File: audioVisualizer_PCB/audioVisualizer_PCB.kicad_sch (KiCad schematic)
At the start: 26 parts, among them J1 Microphone_Module, J2 USB_B_Micro, J3 SPI_MATRIX, J4 JTAG, U1 STM32F103C8Tx, U2 HT7333, Y1 8Mhz

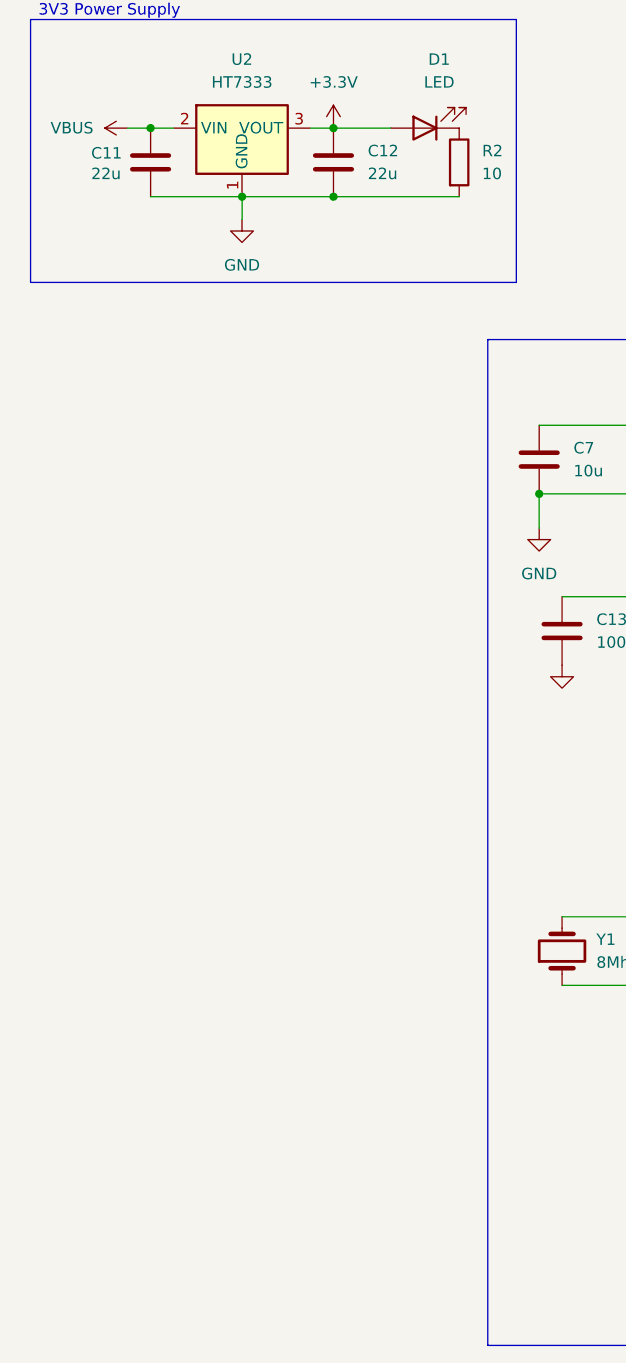
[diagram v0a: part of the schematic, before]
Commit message: Added additional omni-directional smd mic, not routed or programmed
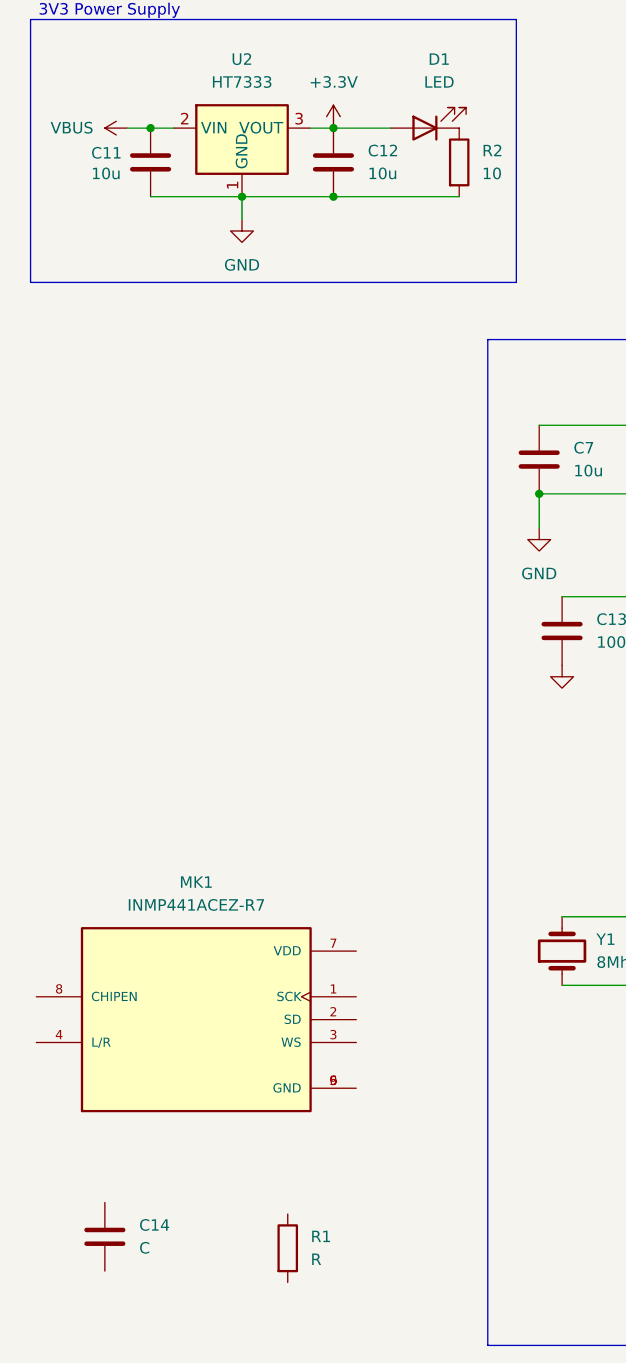
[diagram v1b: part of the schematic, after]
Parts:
- added C14: C, Capacitor_SMD:C_0805_2012Metric, symbol Device:C
- added MK1: INMP441ACEZ-R7, Microphone:MIC_INMP441ACEZ-R7, symbol Microphone:INMP441ACEZ-R7
- added R1: R, Resistor_SMD:R_0805_2012Metric, symbol Device:R
- C11, C12: value 22u -> 10u
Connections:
- new net: MK1.5 (GND), MK1.6 (GND), MK1.9 (GND)

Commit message: break em out
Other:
- added sheet MAX_Controller (MAX_Controller.kicad_sch)
- moved on the sheet: C14, MK1, R1
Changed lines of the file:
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@@
 	(symbol
 		(lib_id "Microphone:INMP441ACEZ-R7")
-		(at 36.83 128.27 0)
+		(at 41.91 93.98 0)
 		(unit 1)
 		(exclude_from_sim no)
@@
 		(fields_autoplaced yes)
 		(property "Reference" "MK1"
-			(at 36.83 113.03 0)
+			(at 41.91 78.74 0)
 			(effects
 				(font
@@
 		)
 		(property "Value" "INMP441ACEZ-R7"
-			(at 36.83 115.57 0)
+			(at 41.91 81.28 0)
 			(effects
 				(font
@@
 		)
 		(property "Footprint" "Microphone:MIC_INMP441ACEZ-R7"
-			(at 36.83 128.27 0)
+			(at 41.91 93.98 0)
 			(effects
 				(font
@@
 		)
 		(property "Datasheet" ""
-			(at 36.83 128.27 0)
+			(at 41.91 93.98 0)
 			(effects
 				(font
@@
 		)
 		(property "Description" ""
-			(at 36.83 128.27 0)
+			(at 41.91 93.98 0)
 			(effects
 				(font
@@
 		)
 		(property "MF" "TDK InvenSense"
-			(at 36.83 128.27 0)
+			(at 41.91 93.98 0)
 			(effects
 				(font
@@
 		)
 		(property "MAXIMUM_PACKAGE_HEIGHT" "1.05 mm"
-			(at 36.83 128.27 0)
+			(at 41.91 93.98 0)
 			(effects
 				(font
@@
 		)
 		(property "Package" "LGA-9 TDK InvenSense"
-			(at 36.83 128.27 0)
+			(at 41.91 93.98 0)
 			(effects
 				(font
@@
 		)
 		(property "Price" "None"
-			(at 36.83 128.27 0)
+			(at 41.91 93.98 0)
 			(effects
 				(font
@@
 		)
 		(property "Check_prices" "https://www.snapeda.com/parts/INMP441ACEZ-R7/TDK/view-part/?ref=eda"
-			(at 36.83 128.27 0)
+			(at 41.91 93.98 0)
 			(effects
 				(font
@@
 		)
 		(property "STANDARD" "Manufacturer Recommendations"
-			(at 36.83 128.27 0)
+			(at 41.91 93.98 0)
 			(effects
 				(font
@@
 		)
 		(property "PARTREV" "1.1"
-			(at 36.83 128.27 0)
+			(at 41.91 93.98 0)
 			(effects
 				(font
@@
 		)
 		(property "SnapEDA_Link" "https://www.snapeda.com/parts/INMP441ACEZ-R7/TDK/view-part/?ref=snap"
-			(at 36.83 128.27 0)
+			(at 41.91 93.98 0)
 			(effects
 				(font
@@
 		)
 		(property "MP" "INMP441ACEZ-R7"
-			(at 36.83 128.27 0)
+			(at 41.91 93.98 0)
 			(effects
 				(font
@@
 		)
 		(property "Description_1" "60 Hz ~ 15 kHz Digital, I2S Microphone MEMS (Silicon) 1.62 V ~ 3.63 V Omnidirectional (-26dB ±3dB @ 94dB SPL) Solder Pads"
-			(at 36.83 128.27 0)
+			(at 41.91 93.98 0)
 			(effects
 				(font
@@
 		)
 		(property "Availability" "In Stock"
-			(at 36.83 128.27 0)
+			(at 41.91 93.98 0)
 			(effects
 				(font
@@
 		)
 		(property "MANUFACTURER" "TDK InvenSense"
-			(at 36.83 128.27 0)
+			(at 41.91 93.98 0)
 			(effects
 				(font
@@
 	(symbol
 		(lib_id "Device:C")
-		(at 26.67 152.4 0)
+		(at 31.75 118.11 0)
 		(unit 1)
 		(exclude_from_sim no)
@@
 		(fields_autoplaced yes)
 		(property "Reference" "C14"
-			(at 30.48 151.1299 0)
+			(at 35.56 116.8399 0)
 			(effects
 				(font
@@
 		)
 		(property "Value" "C"
-			(at 30.48 153.6699 0)
+			(at 35.56 119.3799 0)
 			(effects
 				(font
@@
 		)
 		(property "Footprint" "Capacitor_SMD:C_0805_2012Metric"
-			(at 27.6352 156.21 0)
+			(at 32.7152 121.92 0)
 			(effects
 				(font
@@
 		)
 		(property "Datasheet" "~"
-			(at 26.67 152.4 0)
+			(at 31.75 118.11 0)
 			(effects
 				(font
@@
 		)
 		(property "Description" "Unpolarized capacitor"
-			(at 26.67 152.4 0)
+			(at 31.75 118.11 0)
 			(effects
 				(font
@@
 	(symbol
 		(lib_id "Device:R")
-		(at 46.99 153.67 0)
+		(at 52.07 119.38 0)
 		(unit 1)
 		(exclude_from_sim no)
@@
 		(fields_autoplaced yes)
 		(property "Reference" "R1"
-			(at 49.53 152.3999 0)
+			(at 54.61 118.1099 0)
 			(effects
 				(font
@@
 		)
 		(property "Value" "R"
-			(at 49.53 154.9399 0)
+			(at 54.61 120.6499 0)
 			(effects
 				(font
@@
 		)
 		(property "Footprint" "Resistor_SMD:R_0805_2012Metric"
-			(at 45.212 153.67 90)
+			(at 50.292 119.38 90)
 			(effects
 				(font
@@
 		)
 		(property "Datasheet" "~"
-			(at 46.99 153.67 0)
+			(at 52.07 119.38 0)
 			(effects
 				(font
@@
 		)
 		(property "Description" "Resistor"
-			(at 46.99 153.67 0)
+			(at 52.07 119.38 0)
 			(effects
 				(font
@@
 				)
 			)
+		)
+	)
+	(sheet
+		(at 29.21 132.08)
+		(size 26.67 22.86)
+		(exclude_from_sim no)
+		(in_bom yes)
+		(on_board yes)
+		(dnp no)
+		(fields_autoplaced yes)
+		(stroke
+			(width 0.1524)
+			(type solid)
+		)
+		(fill
+			(color 0 0 0 0.0000)
+		)
+		(property "Sheetname" "MAX_Controller"
+			(at 29.21 131.3684 0)
+			(effects
+				(font
+					(size 1.27 1.27)
+				)
+				(justify left bottom)
+			)
+		)
+		(property "Sheetfile" "MAX_Controller.kicad_sch"
+			(at 29.21 155.5246 0)
+			(effects
+				(font
+					(size 1.27 1.27)
+				)
+				(justify left top)
+			)
+		)
+		(instances
+			(project "audioVisualizer_PCB"
+				(path "/8779f4c0-fa76-4e9c-9285-12099bba0fb4"
+					(page "2")
+				)
+			)

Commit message: embeddeding the mcu is harder than I thought
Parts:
- removed C2: 20p, Capacitor_SMD:C_0805_2012Metric, symbol Device:C
- removed U1: STM32F103C8Tx, Package_QFP:LQFP-48_7x7mm_P0.5mm, symbol MCU_ST_STM32F1:STM32F103C8Tx
- removed Y1: 8Mhz, Crystal:Crystal_HC49-4H_Vertical, symbol Device:Crystal
- added U7: STM32F401CCUx, Package_DFN_QFN:QFN-48-1EP_7x7mm_P0.5mm_EP5.6x5.6mm, symbol MCU_ST_STM32F4:STM32F401CCUx
- added Y2: Crystal_GND23, Crystal:Crystal_SMD_3225-4Pin_3.2x2.5mm, symbol Device:Crystal_GND23
- C1: value 20p -> 15pF; footprint Capacitor_SMD:C_0805_2012Metric -> (none)
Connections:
- net +3.3V: now also U7.1 (VBAT), U7.24 (VDD), U7.36 (VDD), U7.48 (VDD), Y2.1, Y2.4
- net GND: now also C1.2, U7.23 (VSS), U7.35 (VSS), U7.47 (VSS), U7.49 (VSS), U7.8 (VSSA); no longer C1.1
- new net: C1.1, U7.5 (PH0), Y2.3 (G)

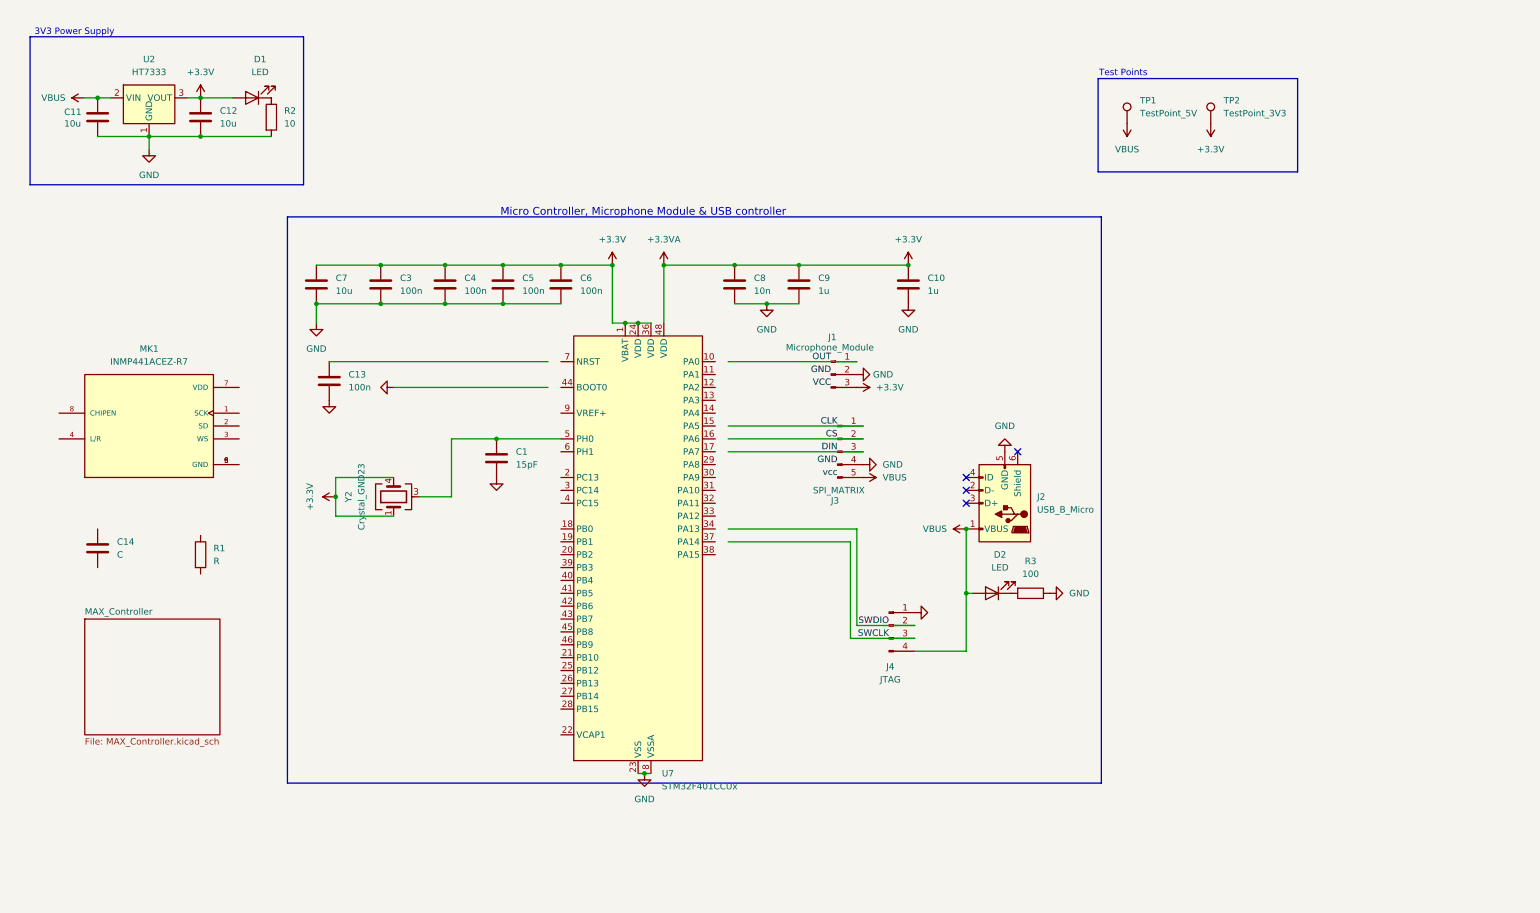
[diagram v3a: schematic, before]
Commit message: added stereo mics; setup usb-c;fixed timer issue for led matrix; using external clock
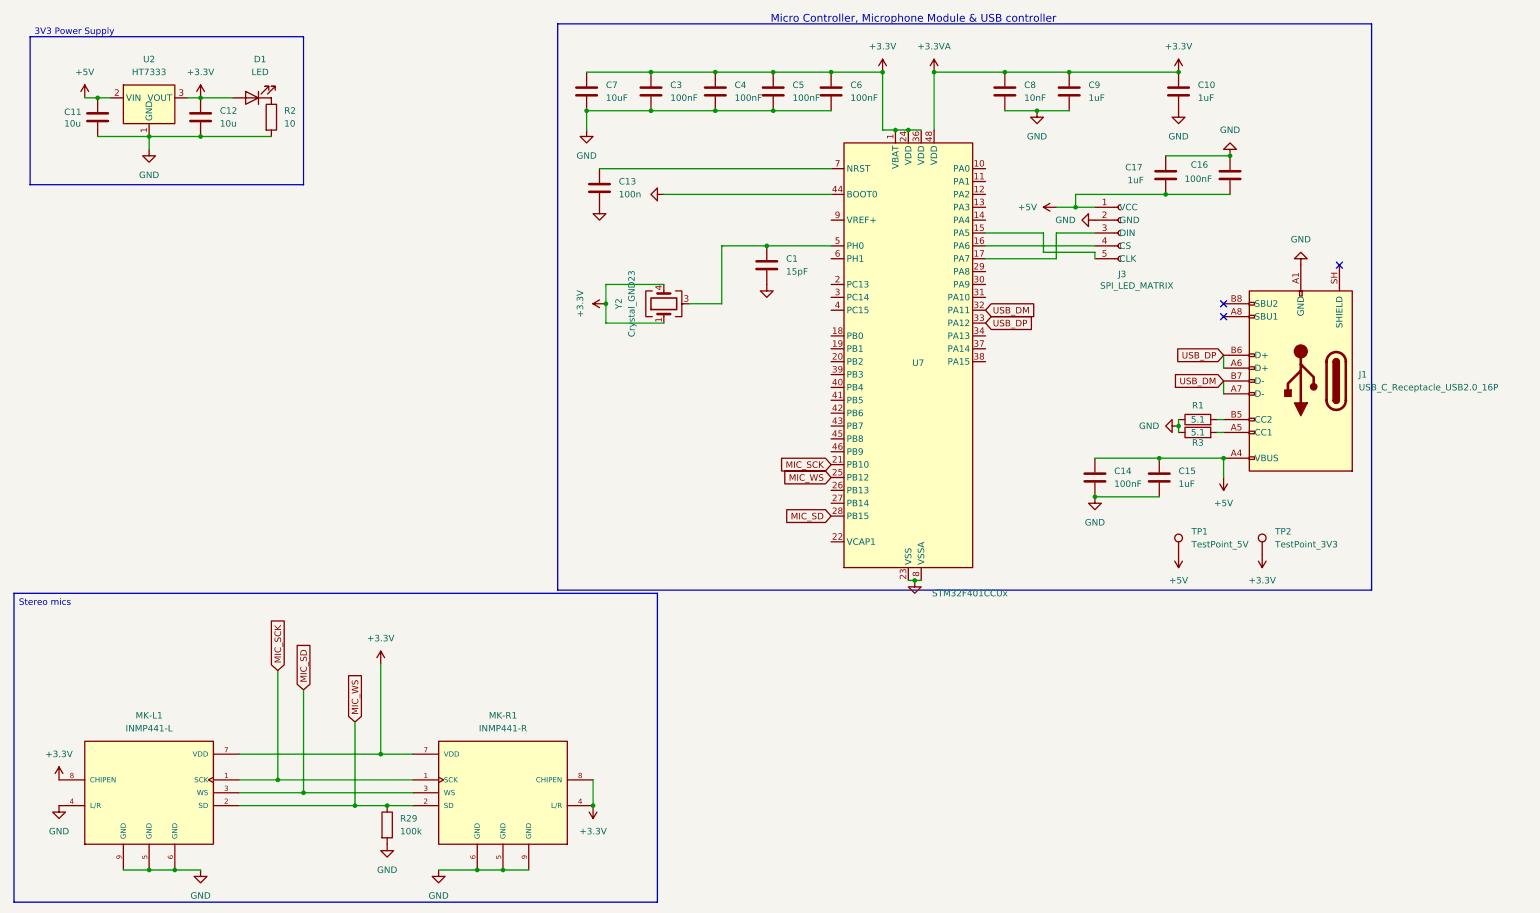
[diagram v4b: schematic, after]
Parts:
- removed D2: LED, LED_SMD:LED_0805_2012Metric, symbol Device:LED
- removed J1: Microphone_Module, Connector_PinHeader_2.54mm:PinHeader_1x03_P2.54mm_Horizontal, symbol Connector:Conn_01x03_Pin
- removed J2: USB_B_Micro, Connector_USB:USB_Micro-B_Amphenol_10118193-0001LF_Horizontal, symbol Connector:USB_B_Micro
- removed J3: SPI_MATRIX, Connector_PinSocket_2.54mm:PinSocket_1x05_P2.54mm_Vertical, symbol Connector:Conn_01x05_Pin
- removed J4: JTAG, Connector_PinHeader_2.54mm:PinHeader_1x04_P2.54mm_Vertical, symbol Connector:Conn_01x04_Pin
- removed MK1: INMP441ACEZ-R7, Microphone:MIC_INMP441ACEZ-R7, symbol Microphone:INMP441ACEZ-R7
- added C15, C17: 1uF, symbol Device:C
- added C16: 100nF, symbol Device:C
- added J1: USB_C_Receptacle_USB2.0_16P, Connector_USB:USB_C_Receptacle_GCT_USB4105-xx-A_16P_TopMnt_Horizontal, symbol Connector:USB_C_Receptacle_USB2.0_16P
- added J3: SPI_LED_MATRIX, symbol Connector:Conn_01x05_Socket
- added MK-L1: INMP441-L, Audio_Module:MIC_INMP441ACEZ-R7, symbol Microphone:INMP441ACEZ-R7
- added MK-R1: INMP441-R, Audio_Module:MIC_INMP441ACEZ-R7, symbol Microphone:INMP441ACEZ-R7
- added R29: 100k, Resistor_SMD:R_0805_2012Metric, symbol Device:R
- C10, C9: value 1u -> 1uF
- C14: value C -> 100nF; footprint Capacitor_SMD:C_0805_2012Metric -> (none)
- C3, C4, C5, C6: value 100n -> 100nF
- C7: value 10u -> 10uF
- C8: value 10n -> 10nF
- R1: value R -> 5.1; footprint Resistor_SMD:R_0805_2012Metric -> (none)
- R3: value 100 -> 5.1; footprint Resistor_SMD:R_0805_2012Metric -> (none)
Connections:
- net VBUS is gone; now on net +5V: C11.1, TP1.1, U2.2 (VIN)
- net +3.3V: now also MK-L1.7 (VDD), MK-L1.8 (CHIPEN), MK-R1.4 (L/R), MK-R1.7 (VDD), MK-R1.8 (CHIPEN)
- net GND: now also C14.1, R1.1, U7.44 (BOOT0), C15.2, C16.1, C17.2, J1.A1 (GND), J1.A12 (GND), J1.B1 (GND), J1.B12 (GND), J3.2 (GND), MK-L1.4 (L/R), MK-L1.5 (GND), MK-L1.6 (GND), MK-L1.9 (GND), MK-R1.5 (GND), MK-R1.6 (GND), MK-R1.9 (GND), R29.2
- net at U7.15 (PA5): now also J3.5 (CLK)
- net at U7.16 (PA6): now also J3.4 (CS)
- net at U7.17 (PA7): now also J3.3 (DIN)
- net MIC_SCK: now reaches U7.21 (PB10)
- net MIC_SCK: now also MK-L1.1 (SCK), MK-R1.1 (SCK)
- net MIC_WS: now reaches U7.25 (PB12)
- net MIC_WS: now also MK-L1.2 (SD), MK-R1.2 (SD), R29.1
- net MIC_SD: now reaches U7.28 (PB15)
- net MIC_SD: now also MK-L1.3 (WS), MK-R1.3 (WS)
- net USB_DM: now reaches U7.32 (PA11)
- net USB_DM: now also J1.A7 (D-), J1.B7 (D-)
- net USB_DP: now reaches U7.33 (PA12)
- net USB_DP: now also J1.A6 (D+), J1.B6 (D+)
- net at U7.7 (NRST): now also C13.1
- net at R3.2: now also J1.A5 (CC1)
- net +5V: now reaches C14.2
- net +5V: now also C15.1, C16.2, C17.1, J1.A4 (VBUS), J1.A9 (VBUS), J1.B4 (VBUS), J1.B9 (VBUS), J3.1 (VCC)
- net at R1.2: now also J1.B5 (CC2)
- no-connect marks 4 -> 3
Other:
- removed sheet MAX_Controller
- note removed: "Test Points"
- moved on the sheet: C1, C10, C13, C3, C4, C5, C6, C7, C8, C9, U7, Y2

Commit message: finished pcb ready for production
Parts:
- removed Y2: Crystal_GND23, Crystal:Crystal_SMD_3225-4Pin_3.2x2.5mm, symbol Device:Crystal_GND23
- added GND: TestPoint_5V, TestPoint:TestPoint_Pad_1.0x1.0mm, symbol Connector:TestPoint
- added TP3: SWDIO, TestPoint:TestPoint_Pad_1.0x1.0mm, symbol Connector:TestPoint
- added TP4: SWCLK, TestPoint:TestPoint_Pad_1.0x1.0mm, symbol Connector:TestPoint
- added Y1: ASE-25MHz, Oscillator:Oscillator_SMD_Abracon_ASE-4Pin_3.2x2.5mm, symbol Oscillator:ASE-xxxMHz
- C1, C14, C15, C16, C17: footprint (none) -> Capacitor_SMD:C_0805_2012Metric
- J3: footprint (none) -> Connector_PinSocket_2.54mm:PinSocket_1x05_P2.54mm_Vertical
- MK-L1, MK-R1: footprint Audio_Module:MIC_INMP441ACEZ-R7 -> Custom:MIC_INMP441ACEZ-R7
- R1, R3: footprint (none) -> Resistor_SMD:R_0805_2012Metric
- renumbered TP2 to 3V3, TP1 to 5V
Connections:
- net +3.3V: now also Y1.1 (EN), Y1.4 (Vdd)
- net GND: now also GND.1, Y1.2 (GND)
- net at U7.34 (PA13): now also TP3.1
- net at U7.37 (PA14): now also TP4.1
- net at C1.1, U7.5 (PH0): now also Y1.3 (OUT)

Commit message: reflect on code as well
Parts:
- renumbered 5V to 5V1, GND to GND1
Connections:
- net at U7.16 (PA6): no longer J3.4 (CS)
- net SPI_CS: now reaches U7.27 (PB14)
- net SPI_CS: now also J3.4 (CS)
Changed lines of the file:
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@@
 	(wire
 		(pts
+			(xy 227.33 62.23) (xy 227.33 60.96)
+		)
+		(stroke
+			(width 0)
+			(type default)
+		)
+	)
+	(wire
+		(pts
 			(xy 140.97 31.75) (xy 153.67 31.75)
 		)
@@
 	(wire
 		(pts
-			(xy 220.98 55.88) (xy 220.98 60.96)
+			(xy 215.9 55.88) (xy 215.9 60.96)
 		)
 		(stroke
@@
 	(wire
 		(pts
-			(xy 228.6 58.42) (xy 207.01 58.42)
-		)
-		(stroke
-			(width 0)
-			(type default)
-		)
-	)
-	(wire
-		(pts
 			(xy 128.27 62.23) (xy 138.43 62.23)
 		)
@@
 	(wire
 		(pts
-			(xy 218.44 59.69) (xy 218.44 55.88)
+			(xy 214.63 62.23) (xy 214.63 55.88)
 		)
 		(stroke
@@
 	(wire
 		(pts
-			(xy 218.44 55.88) (xy 207.01 55.88)
-		)
-		(stroke
-			(width 0)
-			(type default)
-		)
-	)
-	(wire
-		(pts
-			(xy 228.6 59.69) (xy 228.6 60.96)
+			(xy 214.63 55.88) (xy 207.01 55.88)
 		)
 		(stroke
@@
 	(wire
 		(pts
-			(xy 220.98 60.96) (xy 207.01 60.96)
+			(xy 215.9 60.96) (xy 207.01 60.96)
 		)
 		(stroke
@@
 	(wire
 		(pts
-			(xy 228.6 55.88) (xy 220.98 55.88)
+			(xy 228.6 55.88) (xy 215.9 55.88)
 		)
 		(stroke
@@
 	(wire
 		(pts
-			(xy 228.6 59.69) (xy 218.44 59.69)
+			(xy 214.63 62.23) (xy 227.33 62.23)
 		)
 		(stroke
@@
 	(wire
 		(pts
+			(xy 227.33 60.96) (xy 228.6 60.96)
+		)
+		(stroke
+			(width 0)
+			(type default)
+		)
+	)
+	(wire
+		(pts
 			(xy 29.21 29.21) (xy 31.75 29.21)
 		)
@@
 		)
 	)
+	(global_label "SPI_CS"
+		(shape input)
+		(at 176.53 109.22 180)
+		(fields_autoplaced yes)
+		(effects
+			(font
+				(size 1.27 1.27)
+			)
+			(justify right)
+		)
+		(property "Intersheetrefs" "${INTERSHEET_REFS}"
+			(at 167.0134 109.22 0)
+			(hide yes)
+			(show_name no)
+			(do_not_autoplace no)
+			(effects
+				(font
+					(size 1.27 1.27)
+				)
+				(justify right)
+			)
+		)
+	)
 	(global_label "MIC_SCK"
 		(shape input)
@@
 		)
 	)
+	(global_label "SPI_CS"
+		(shape input)
+		(at 228.6 58.42 180)
+		(fields_autoplaced yes)
+		(effects
+			(font
+				(size 1.27 1.27)
+			)
+			(justify right)
+		)
+		(property "Intersheetrefs" "${INTERSHEET_REFS}"
+			(at 219.0834 58.42 0)
+			(hide yes)
+			(show_name no)
+			(do_not_autoplace no)
+			(effects
+				(font
+					(size 1.27 1.27)
+				)
+				(justify right)
+			)
+		)
+	)
 	(global_label "USB_DM"
 		(shape input)
@@
 		(dnp no)
 		(fields_autoplaced yes)
-		(property "Reference" "GND"
+		(property "Reference" "GND1"
 			(at 234.95 114.8079 0)
 			(show_name no)
@@
 			(project "audioVisualizer_PCB"
 				(path "/8779f4c0-fa76-4e9c-9285-12099bba0fb4"
-					(reference "GND")
+					(reference "GND1")
 					(unit 1)
 				)
@@
 		(dnp no)
 		(fields_autoplaced yes)
-		(property "Reference" "5V"
+		(property "Reference" "5V1"
 			(at 247.65 114.8079 0)
 			(show_name no)
@@
 			(project "audioVisualizer_PCB"
 				(path "/8779f4c0-fa76-4e9c-9285-12099bba0fb4"
-					(reference "5V")
+					(reference "5V1")
 					(unit 1)
 				)
